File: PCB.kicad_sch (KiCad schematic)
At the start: 84 parts, among them J1 USB_C_Receptacle_USB2.0_16P, J10 Conn_01x02_Pin, J11 Conn_01x05_Pin, J12 Conn_01x02_Pin, J13 Conn_01x04_Pin, J14 Conn_01x04_Pin, J15 Conn_01x02_Pin, J16 Conn_01x05_Pin, J17 Conn_01x03_Pin, J18 Conn_01x03_Pin, J19 Conn_01x03_Pin, J2 Conn_01x11_Socket, J20 Conn_01x03_Pin, J21 Conn_01x05_Pin, J22 Conn_01x04_Pin, J23 Conn_01x03_Pin, J24 Conn_01x03_Pin, J26 Conn_01x03_Pin, J27 Conn_01x02_Pin, J3 Conn_01x08_Socket, J4 Conn_01x11_Socket, J5 Conn_01x02_Pin, J6 Conn_01x02_Pin, J7 Conn_01x02_Pin, J8 Conn_01x03_Pin, J9 Conn_01x02_Pin, SW1 SW_Push, SW2 SW_Push, U10 MCP23008-xSO, U2 LTC4412xS6, U3 LTC4412xS6, U4 AMS1117-3.3 (UMW), U6 ESP32-S3-WROOM-1, U7 TMC2209_SILENTSTEPSTICK, U8 TMC2209_SILENTSTEPSTICK, U9 TMC2209_SILENTSTEPSTICK

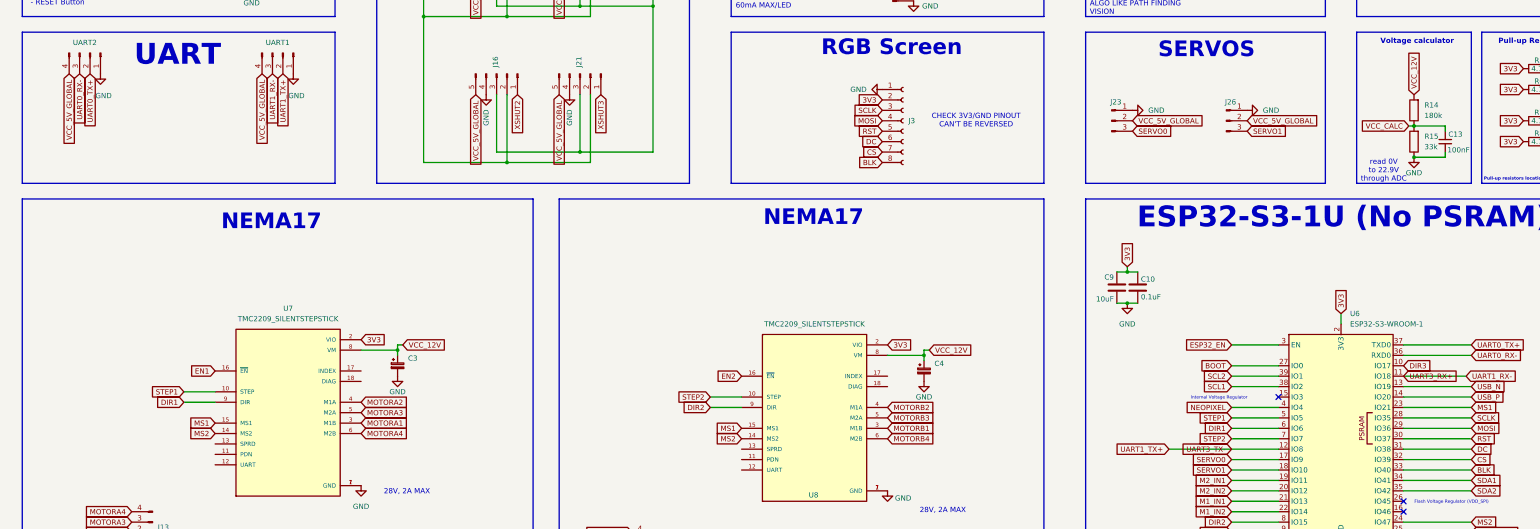
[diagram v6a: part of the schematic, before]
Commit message: suite routage + séparation 2eme pcb avec 2 nema
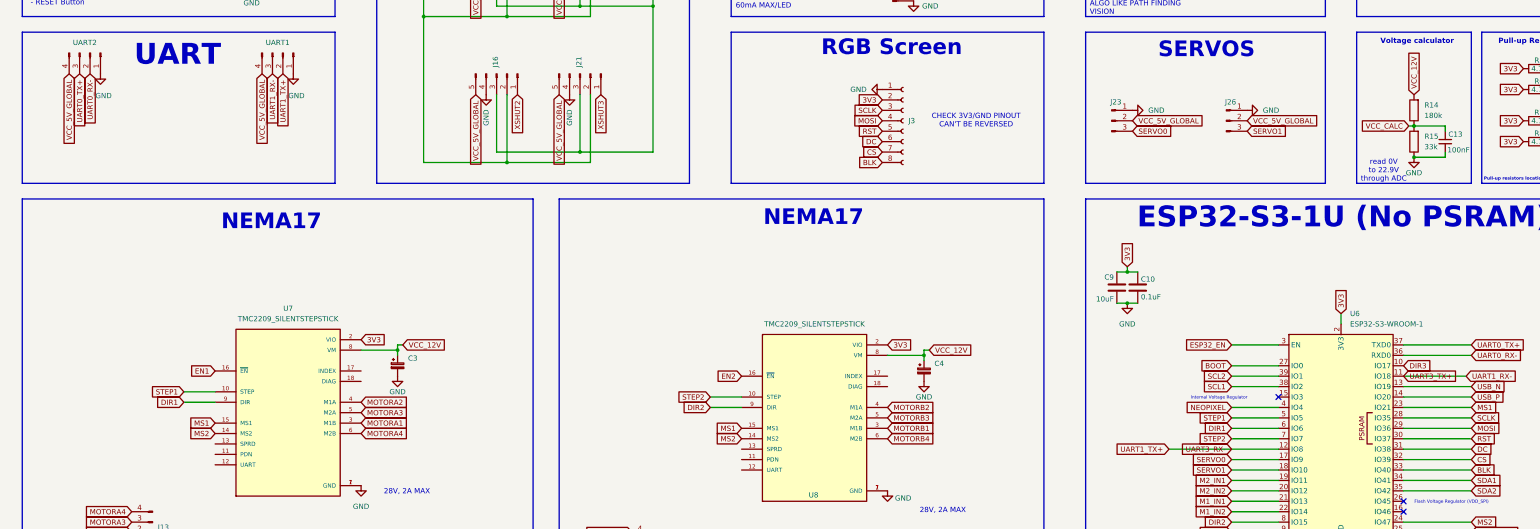
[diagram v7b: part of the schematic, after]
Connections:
- net UART3_RX- is gone; now on net UART1_TX+: J2.2 (Pin_2)
- net UART3_TX+ is gone; now on net UART1_RX-: J2.1 (Pin_1)
- net UART0_RX-: now also UART2.2 (Pin_2); no longer UART2.3 (Pin_3)
- net UART0_TX+: now also UART2.3 (Pin_3); no longer UART2.2 (Pin_2)
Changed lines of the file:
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@@
 		)
 	)
-	(global_label "UART0_RX-"
-		(shape input)
-		(at 29.21 152.4 270)
-		(fields_autoplaced yes)
-		(effects
-			(font
-				(size 1.27 1.27)
-			)
-			(justify right)
-		)
-		(property "Intersheetrefs" "${INTERSHEET_REFS}"
-			(at 29.21 166.2709 90)
-			(hide yes)
-			(show_name no)
-			(do_not_autoplace no)
-			(effects
-				(font
-					(size 1.27 1.27)
-				)
-				(justify right)
-			)
-		)
-	)
 	(global_label "SCL2"
 		(shape input)
@@
 		)
 	)
-	(global_label "UART3_RX+"
-		(shape input)
-		(at 351.79 226.06 0)
-		(fields_autoplaced yes)
-		(effects
-			(font
-				(size 1.27 1.27)
-			)
-			(justify left)
-		)
-		(property "Intersheetrefs" "${INTERSHEET_REFS}"
-			(at 365.6609 226.06 0)
-			(hide yes)
-			(show_name no)
-			(do_not_autoplace no)
-			(effects
-				(font
-					(size 1.27 1.27)
-				)
-				(justify left)
-			)
-		)
-	)
 	(global_label "XSHUT1"
 		(shape input)
@@
 		)
 	)
+	(global_label "UART0_TX+"
+		(shape input)
+		(at 29.21 152.4 270)
+		(fields_autoplaced yes)
+		(effects
+			(font
+				(size 1.27 1.27)
+			)
+			(justify right)
+		)
+		(property "Intersheetrefs" "${INTERSHEET_REFS}"
+			(at 29.21 165.9685 90)
+			(hide yes)
+			(show_name no)
+			(do_not_autoplace no)
+			(effects
+				(font
+					(size 1.27 1.27)
+				)
+				(justify right)
+			)
+		)
+	)
 	(global_label "XSHUT0"
 		(shape input)
@@
 		)
 	)
-	(global_label "UART3_TX-"
-		(shape input)
-		(at 309.88 243.84 180)
-		(fields_autoplaced yes)
-		(effects
-			(font
-				(size 1.27 1.27)
-			)
-			(justify right)
-		)
-		(property "Intersheetrefs" "${INTERSHEET_REFS}"
-			(at 296.3115 243.84 0)
-			(hide yes)
-			(show_name no)
-			(do_not_autoplace no)
-			(effects
-				(font
-					(size 1.27 1.27)
-				)
-				(justify right)
-			)
-		)
-	)
 	(global_label "MS1"
 		(shape input)
@@
 		)
 	)
-	(global_label "UART0_TX+"
+	(global_label "SCL1"
 		(shape input)
-		(at 31.75 152.4 270)
+		(at 439.42 127 180)
 		(fields_autoplaced yes)
 		(effects
@@
 		)
 		(property "Intersheetrefs" "${INTERSHEET_REFS}"
-			(at 31.75 165.9685 90)
+			(at 431.7177 127 0)
 			(hide yes)
 			(show_name no)
@@
 		)
 	)
-	(global_label "SCL1"
+	(global_label "MS2"
 		(shape input)
-		(at 439.42 127 180)
+		(at 190.5 342.9 180)
 		(fields_autoplaced yes)
 		(effects
@@
 		)
 		(property "Intersheetrefs" "${INTERSHEET_REFS}"
-			(at 431.7177 127 0)
+			(at 183.6444 342.9 0)
 			(hide yes)
 			(show_name no)
@@
 		)
 	)
-	(global_label "MS2"
+	(global_label "UART3_RX-"
 		(shape input)
-		(at 190.5 342.9 180)
+		(at 309.88 243.84 180)
 		(fields_autoplaced yes)
 		(effects
@@
 		)
 		(property "Intersheetrefs" "${INTERSHEET_REFS}"
-			(at 183.6444 342.9 0)
+			(at 296.0091 243.84 0)
 			(hide yes)
 			(show_name no)
@@
 		)
 	)
+	(global_label "UART3_TX+"
+		(shape input)
+		(at 351.79 226.06 0)
+		(fields_autoplaced yes)
+		(effects
+			(font
+				(size 1.27 1.27)
+			)
+			(justify left)
+		)
+		(property "Intersheetrefs" "${INTERSHEET_REFS}"
+			(at 365.3585 226.06 0)
+			(hide yes)
+			(show_name no)
+			(do_not_autoplace no)
+			(effects
+				(font
+					(size 1.27 1.27)
+				)
+				(justify left)
+			)
+		)
+	)
 	(global_label "TEAM_BTN"
 		(shape input)
@@
 			)
 		)
+	)
+	(global_label "UART0_RX-"
+		(shape input)
+		(at 31.75 152.4 270)
+		(fields_autoplaced yes)
+		(effects
+			(font
+				(size 1.27 1.27)
+			)
+			(justify right)
+		)
+		(property "Intersheetrefs" "${INTERSHEET_REFS}"
+			(at 31.75 166.2709 90)
+			(hide yes)
+			(show_name no)
+			(do_not_autoplace no)
+			(effects
+				(font
+					(size 1.27 1.27)
+				)
+				(justify right)
+			)
+		)
